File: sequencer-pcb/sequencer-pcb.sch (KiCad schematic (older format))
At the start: 39 parts, among them SW1 SW_Push, SW10 SW_Push, SW11 SW_Push, SW2 SW_Push, SW3 SW_Push, SW4 SW_Push, SW5 SW_Push, SW6 SW_Push, SW7 SW_Push, SW8 SW_Push, SW9 SW_Push, U1 STM32F103C8Tx

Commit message: pcb changes
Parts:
- removed U?: 4051, symbol 4xxx:4051
- added J?: Conn_01x02_Female, symbol Connector:Conn_01x02_Female
- added J?: Conn_02x10_Counter_Clockwise, symbol Connector_Generic:Conn_02x10_Counter_Clockwise
- added J?: Conn_02x08_Counter_Clockwise, symbol Connector_Generic:Conn_02x08_Counter_Clockwise
- added R? (x17): R, symbol Device:R
- added RV?: R_POT_TRIM, symbol Device:R_POT_TRIM
- added TP? (x2): TestPoint, symbol Connector:TestPoint
- added U?: 74HC164, symbol 74xx:74HC164
- renumbered RV3 to RV2, RV5 to RV3, RV7 to RV4, RV2 to RV5, RV4 to RV6, RV6 to RV7
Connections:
- net labels added: +5V, GND, L1, L2, L3, L4, L5, L6, L7, L8, R1, R2, R3, R4, R5, R6, R7, R8
- wire segments 0 -> 123
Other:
- moved on the sheet: D1, D2, D3, D4, D5, D6, D7, D8, D9, J?, RV1, RV10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

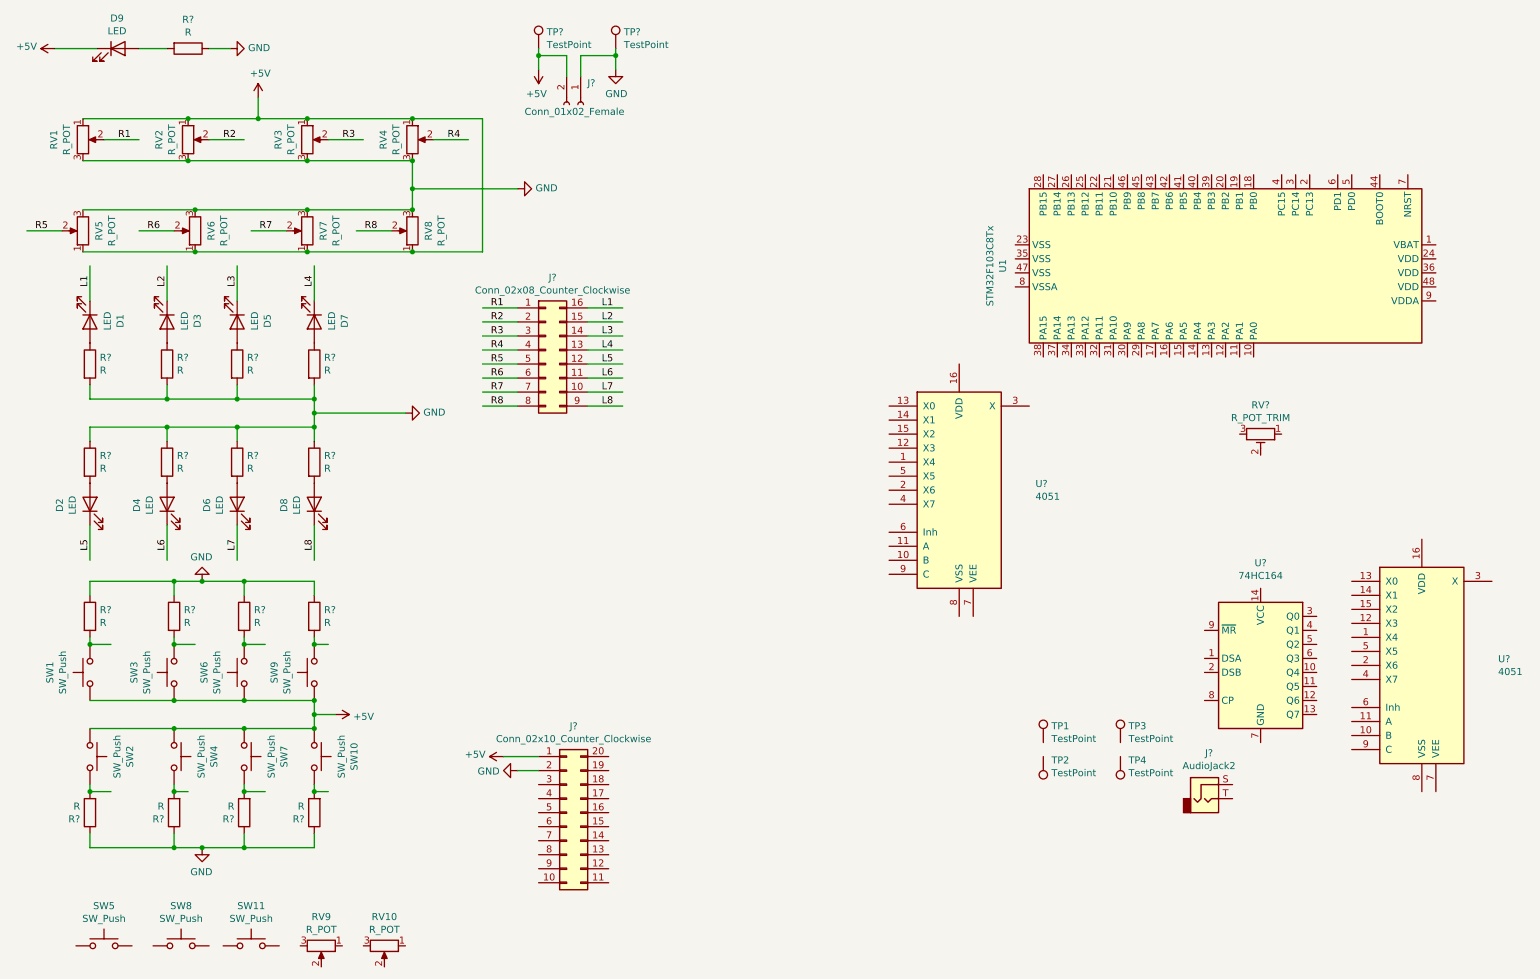
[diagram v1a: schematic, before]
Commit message: updates pcb and schematic
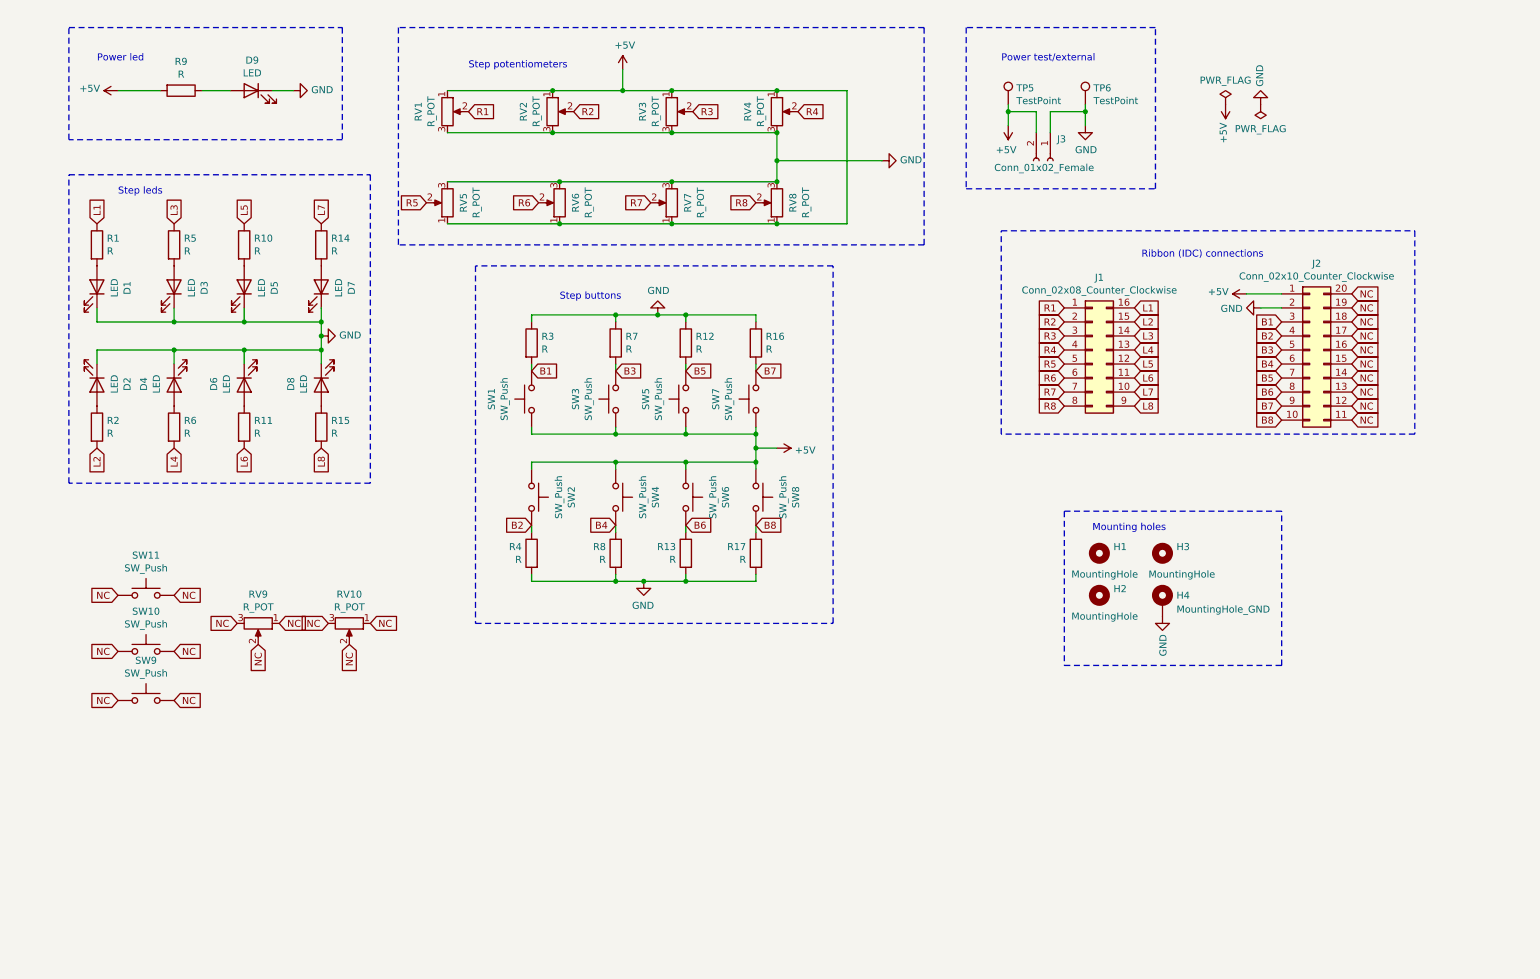
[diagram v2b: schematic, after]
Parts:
- removed J?: AudioJack2, symbol Connector:AudioJack2
- removed J?: Conn_02x10_Counter_Clockwise, symbol Connector_Generic:Conn_02x10_Counter_Clockwise
- removed J?: Conn_02x08_Counter_Clockwise, symbol Connector_Generic:Conn_02x08_Counter_Clockwise
- removed RV?: R_POT_TRIM, symbol Device:R_POT_TRIM
- removed SW5, SW8: SW_Push, symbol Switch:SW_Push
- removed TP1, TP2, TP3, TP4: TestPoint, symbol Connector:TestPoint
- removed U1: STM32F103C8Tx, Package_QFP:LQFP-48_7x7mm_P0.5mm, symbol MCU_ST_STM32F1:STM32F103C8Tx
- removed U? (x2): 4051, symbol 4xxx:4051
- removed U?: 74HC164, symbol 74xx:74HC164
- added H1, H2, H3: MountingHole, MountingHole:MountingHole_2.7mm_M2.5, symbol Mechanical:MountingHole
- added H4: MountingHole_GND, MountingHole:MountingHole_2.7mm_M2.5_Pad, symbol Mechanical:MountingHole_Pad
- added J1: Conn_02x08_Counter_Clockwise, Connector_IDC:IDC-Header_2x08_P2.54mm_Vertical, symbol Connector_Generic:Conn_02x08_Counter_Clockwise
- added J2: Conn_02x10_Counter_Clockwise, Connector_IDC:IDC-Header_2x10_P2.54mm_Vertical, symbol Connector_Generic:Conn_02x10_Counter_Clockwise
- added SW10, SW9: SW_Push, Button_Switch_THT:SW_PUSH_6mm, symbol Switch:SW_Push
- D1, D2, D3, D4, D5, D6, D7, D8, D9: footprint (none) -> LED_THT:LED_D5.0mm
- J3: renamed from J?; footprint (none) -> Connector_PinHeader_2.54mm:PinHeader_1x02_P2.54mm_Vertical
- R1, R10, R11, R12, R13, R14, R15, R16, R17, R2, R3, R4, R5, R6, R7, R8, R9: renamed from R?; footprint (none) -> Resistor_SMD:R_1806_4516Metric_Pad1.57x1.80mm_HandSolder
- RV1, RV10, RV2, RV3, RV4, RV5, RV6, RV7, RV8, RV9: footprint (none) -> Potentiometer_THT:Potentiometer_Alps_RK09K_Single_Vertical
- SW1, SW11, SW2, SW3, SW4: footprint (none) -> Button_Switch_THT:SW_PUSH_6mm
- SW5: renamed from SW6; footprint (none) -> Button_Switch_THT:SW_PUSH_6mm
- SW6: renamed from SW7; footprint (none) -> Button_Switch_THT:SW_PUSH_6mm
- SW7: renamed from SW9; footprint (none) -> Button_Switch_THT:SW_PUSH_6mm
- SW8: renamed from SW10; footprint (none) -> Button_Switch_THT:SW_PUSH_6mm
- TP5, TP6: renamed from TP?; footprint (none) -> TestPoint:TestPoint_THTPad_2.5x2.5mm_Drill1.2mm
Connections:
- net labels added: B1, B2, B3, B4, B5, B6, B7, B8, NC
- wire segments 123 -> 90
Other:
- note added: "Mounting holes\n"
- note added: "Power led"
- note added: "Power test/external"
- note added: "Ribbon (IDC) connections"
- note added: "Step buttons"
- note added: "Step leds"
- note added: "Step potentiometers"
- moved on the sheet: D1, D2, D3, D4, D5, D6, D7, D8, D9, J3, R1, R10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

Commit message: updates
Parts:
- added RV11: R_POT, Potentiometer_THT:Potentiometer_Alps_RK09K_Single_Vertical, symbol Device:R_POT
- added SW12, SW13: SW_Push, Button_Switch_THT:SW_PUSH_6mm, symbol Switch:SW_Push
- J1: value Conn_02x08_Counter_Clockwise -> Ribbon; footprint Connector_IDC:IDC-Header_2x08_P2.54mm_Vertical -> Connector_IDC:IDC-Header_2x10_P2.54mm_Vertical; symbol Connector_Generic:Conn_02x08_Counter_Clockwise -> Connector_Generic:Conn_02x10_Counter_Clockwise
- RV1, RV2, RV3, RV4, RV5, RV6, RV7, RV8: value R_POT -> 100k
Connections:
- net +5V: now also J1.17 (Pin_17); no longer J2.1 (Pin_1)
- net B1: now also J2.1 (Pin_1); no longer J2.3 (Pin_3)
- net B2: now also J2.2 (Pin_2); no longer J2.4 (Pin_4)
- net B3: now also J2.3 (Pin_3); no longer J2.5 (Pin_5)
- net B4: now also J2.4 (Pin_4); no longer J2.6 (Pin_6)
- net B5: now also J2.5 (Pin_5); no longer J2.7 (Pin_7)
- net B6: now also J2.6 (Pin_6); no longer J2.8 (Pin_8)
- net B7: now also J2.7 (Pin_7); no longer J2.9 (Pin_9)
- net B8: now also J2.8 (Pin_8); no longer J2.10 (Pin_10)
- net GND: now also J1.18 (Pin_18); no longer J2.2 (Pin_2)
- net L1: now also J1.9 (Pin_9); no longer J1.16 (Pin_16)
- net L2: now also J1.10 (Pin_10); no longer J1.15 (Pin_15)
- net L3: now also J1.11 (Pin_11); no longer J1.14 (Pin_14)
- net L4: now also J1.12 (Pin_12); no longer J1.13 (Pin_13)
- net L5: now also J1.13 (Pin_13); no longer J1.12 (Pin_12)
- net L6: now also J1.14 (Pin_14); no longer J1.11 (Pin_11)
- net L7: now also J1.15 (Pin_15); no longer J1.10 (Pin_10)
- net L8: now also J1.16 (Pin_16); no longer J1.9 (Pin_9)
- net NC: now also J1.19 (Pin_19), J1.20 (Pin_20), J2.10 (Pin_10), J2.9 (Pin_9), RV11.1, RV11.2, RV11.3, SW12.1, SW12.2, SW13.1, SW13.2
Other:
- moved on the sheet: SW10, SW11, SW9
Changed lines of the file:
@@
 L Switch:SW_Push SW11
 U 1 1 5F2CD552
-P 1500 4750
-F 0 "SW11" H 1500 5035 50  0000 C CNN
-F 1 "SW_Push" H 1500 4944 50  0000 C CNN
-F 2 "Button_Switch_THT:SW_PUSH_6mm" H 1500 4950 50  0001 C CNN
-F 3 "~" H 1500 4950 50  0001 C CNN
-	1    1500 4750
+P 1450 5650
+F 0 "SW11" H 1450 5935 50  0000 C CNN
+F 1 "SW_Push" H 1450 5844 50  0000 C CNN
+F 2 "Button_Switch_THT:SW_PUSH_6mm" H 1450 5850 50  0001 C CNN
+F 3 "~" H 1450 5850 50  0001 C CNN
+	1    1450 5650
 	1    0    0    -1
 $EndComp
@@
 P 6000 1950
 F 0 "RV8" V 5885 1950 50  0000 C CNN
-F 1 "R_POT" V 5794 1950 50  0000 C CNN
+F 1 "100k" V 5794 1950 50  0000 C CNN
 F 2 "Potentiometer_THT:Potentiometer_Alps_RK09K_Single_Vertical" H 6000 1950 50  0001 C CNN
 F 3 "~" H 6000 1950 50  0001 C CNN
@@
 P 5250 1950
 F 0 "RV7" V 5135 1950 50  0000 C CNN
-F 1 "R_POT" V 5044 1950 50  0000 C CNN
+F 1 "100k" V 5044 1950 50  0000 C CNN
 F 2 "Potentiometer_THT:Potentiometer_Alps_RK09K_Single_Vertical" H 5250 1950 50  0001 C CNN
 F 3 "~" H 5250 1950 50  0001 C CNN
@@
 P 4450 1950
 F 0 "RV6" V 4335 1950 50  0000 C CNN
-F 1 "R_POT" V 4244 1950 50  0000 C CNN
+F 1 "100k" V 4244 1950 50  0000 C CNN
 F 2 "Potentiometer_THT:Potentiometer_Alps_RK09K_Single_Vertical" H 4450 1950 50  0001 C CNN
 F 3 "~" H 4450 1950 50  0001 C CNN
@@
 P 3650 1950
 F 0 "RV5" V 3535 1950 50  0000 C CNN
-F 1 "R_POT" V 3444 1950 50  0000 C CNN
+F 1 "100k" V 3444 1950 50  0000 C CNN
 F 2 "Potentiometer_THT:Potentiometer_Alps_RK09K_Single_Vertical" H 3650 1950 50  0001 C CNN
 F 3 "~" H 3650 1950 50  0001 C CNN
@@
 P 6000 1300
 F 0 "RV4" V 5793 1300 50  0000 C CNN
-F 1 "R_POT" V 5884 1300 50  0000 C CNN
+F 1 "100k" V 5884 1300 50  0000 C CNN
 F 2 "Potentiometer_THT:Potentiometer_Alps_RK09K_Single_Vertical" H 6000 1300 50  0001 C CNN
 F 3 "~" H 6000 1300 50  0001 C CNN
@@
 P 5250 1300
 F 0 "RV3" V 5043 1300 50  0000 C CNN
-F 1 "R_POT" V 5134 1300 50  0000 C CNN
+F 1 "100k" V 5134 1300 50  0000 C CNN
 F 2 "Potentiometer_THT:Potentiometer_Alps_RK09K_Single_Vertical" H 5250 1300 50  0001 C CNN
 F 3 "~" H 5250 1300 50  0001 C CNN
@@
 P 4400 1300
 F 0 "RV2" V 4193 1300 50  0000 C CNN
-F 1 "R_POT" V 4284 1300 50  0000 C CNN
+F 1 "100k" V 4284 1300 50  0000 C CNN
 F 2 "Potentiometer_THT:Potentiometer_Alps_RK09K_Single_Vertical" H 4400 1300 50  0001 C CNN
 F 3 "~" H 4400 1300 50  0001 C CNN
@@
 P 3650 1300
 F 0 "RV1" V 3443 1300 50  0000 C CNN
-F 1 "R_POT" V 3534 1300 50  0000 C CNN
+F 1 "100k" V 3534 1300 50  0000 C CNN
 F 2 "Potentiometer_THT:Potentiometer_Alps_RK09K_Single_Vertical" H 3650 1300 50  0001 C CNN
 F 3 "~" H 3650 1300 50  0001 C CNN
@@
 L power:GND #PWR03
 U 1 1 5F407ABC
-P 9450 2700
+P 8700 2700
 AR Path="/5F407ABC" Ref="#PWR03"  Part="1"
 AR Path="/5F3DFCD9/5F407ABC" Ref="#PWR?"  Part="1"
-F 0 "#PWR03" H 9450 2450 50  0001 C CNN
-F 1 "GND" V 9455 2572 50  0000 R CNN
-F 2 "" H 9450 2700 50  0001 C CNN
-F 3 "" H 9450 2700 50  0001 C CNN
-	1    9450 2700
-	0    1    1    0
-$EndComp
-Wire Wire Line
-	9600 2700 9450 2700
-Wire Wire Line
-	9350 2600 9600 2600
+F 0 "#PWR03" H 8700 2450 50  0001 C CNN
+F 1 "GND" V 8705 2572 50  0000 R CNN
+F 2 "" H 8700 2700 50  0001 C CNN
+F 3 "" H 8700 2700 50  0001 C CNN
+	1    8700 2700
+	0    -1   -1   0
+$EndComp
+Wire Wire Line
+	8550 2700 8700 2700
+Wire Wire Line
+	8800 2800 8550 2800
 $Comp
 L power:+5V #PWR02
 U 1 1 5F407AC4
-P 9350 2600
+P 8800 2800
 AR Path="/5F407AC4" Ref="#PWR02"  Part="1"
 AR Path="/5F3DFCD9/5F407AC4" Ref="#PWR?"  Part="1"
-F 0 "#PWR02" H 9350 2450 50  0001 C CNN
-F 1 "+5V" V 9365 2728 50  0000 L CNN
-F 2 "" H 9350 2600 50  0001 C CNN
-F 3 "" H 9350 2600 50  0001 C CNN
-	1    9350 2600
-	0    -1   -1   0
-$EndComp
-$Comp
-L Connector_Generic:Conn_02x08_Counter_Clockwise J1
+F 0 "#PWR02" H 8800 2650 50  0001 C CNN
+F 1 "+5V" V 8815 2928 50  0000 L CNN
+F 2 "" H 8800 2800 50  0001 C CNN
+F 3 "" H 8800 2800 50  0001 C CNN
+	1    8800 2800
+	0    1    1    0
+$EndComp
+$Comp
+L Connector_Generic:Conn_02x10_Counter_Clockwise J1
 U 1 1 5F407ACA
-P 8250 3000
+P 8250 2900
 AR Path="/5F407ACA" Ref="J1"  Part="1"
 AR Path="/5F3DFCD9/5F407ACA" Ref="J?"  Part="1"
-F 0 "J1" H 8300 3517 50  0000 C CNN
-F 1 "Conn_02x08_Counter_Clockwise" H 8300 3426 50  0000 C CNN
-F 2 "Connector_IDC:IDC-Header_2x08_P2.54mm_Vertical" H 8250 3000 50  0001 C CNN
-F 3 "~" H 8250 3000 50  0001 C CNN
-	1    8250 3000
+F 0 "J1" H 8300 3417 50  0000 C CNN
+F 1 "Ribbon" H 8300 3326 50  0000 C CNN
+F 2 "Connector_IDC:IDC-Header_2x10_P2.54mm_Vertical" H 8250 2900 50  0001 C CNN
+F 3 "~" H 8250 2900 50  0001 C CNN
+	1    8250 2900
 	1    0    0    -1
 $EndComp
@@
 	1    0    0    -1
 $EndComp
+Text GLabel 8050 2500 0    50   Input ~ 0
+R1
+Text GLabel 8050 2600 0    50   Input ~ 0
+R2
 Text GLabel 8050 2700 0    50   Input ~ 0
-R1
+R3
 Text GLabel 8050 2800 0    50   Input ~ 0
-R2
+R4
 Text GLabel 8050 2900 0    50   Input ~ 0
-R3
+R5
 Text GLabel 8050 3000 0    50   Input ~ 0
-R4
+R6
 Text GLabel 8050 3100 0    50   Input ~ 0
-R5
+R7
 Text GLabel 8050 3200 0    50   Input ~ 0
-R6
+R8
 Text GLabel 8050 3300 0    50   Input ~ 0
-R7
+L1
 Text GLabel 8050 3400 0    50   Input ~ 0
-R8
-Text GLabel 8550 2700 2    50   Input ~ 0
-L1
-Text GLabel 8550 2800 2    50   Input ~ 0
 L2
+Text GLabel 8550 3400 2    50   Input ~ 0
+L3
+Text GLabel 8550 3300 2    50   Input ~ 0
+L4
+Text GLabel 8550 3200 2    50   Input ~ 0
+L5
+Text GLabel 8550 3100 2    50   Input ~ 0
+L6
+Text GLabel 8550 3000 2    50   Input ~ 0
+L7
 Text GLabel 8550 2900 2    50   Input ~ 0
-L3
-Text GLabel 8550 3000 2    50   Input ~ 0
-L4
-Text GLabel 8550 3100 2    50   Input ~ 0
-L5
-Text GLabel 8550 3200 2    50   Input ~ 0
-L6
-Text GLabel 8550 3300 2    50   Input ~ 0
-L7
-Text GLabel 8550 3400 2    50   Input ~ 0
 L8
+Text GLabel 9600 2600 0    50   Input ~ 0
+B1
+Text GLabel 9600 2700 0    50   Input ~ 0
+B2
 Text GLabel 9600 2800 0    50   Input ~ 0
-B1
+B3
 Text GLabel 9600 2900 0    50   Input ~ 0
-B2
+B4
 Text GLabel 9600 3000 0    50   Input ~ 0
-B3
+B5
 Text GLabel 9600 3100 0    50   Input ~ 0
-B4
+B6
 Text GLabel 9600 3200 0    50   Input ~ 0
-B5
+B7
 Text GLabel 9600 3300 0    50   Input ~ 0
-B6
-Text GLabel 9600 3400 0    50   Input ~ 0
-B7
-Text GLabel 9600 3500 0    50   Input ~ 0
 B8
 Text Notes 1150 950  0    50   ~ 0
@@
 	10550 2150 10550 3600
 Wire Notes Line
-	10550 3600 7600 3600
+	7600 3600 10550 3600
 Wire Notes Line
 	7600 3600 7600 2150
@@
 Text GLabel 2150 4950 0    50   Input ~ 0
 NC
-Text GLabel 1700 4750 2    50   Input ~ 0
-NC
-Text GLabel 1300 4750 0    50   Input ~ 0
+Text GLabel 1650 5650 2    50   Input ~ 0
+NC
+Text GLabel 1250 5650 0    50   Input ~ 0
 NC
 $Comp
 L Switch:SW_Push SW10
 U 1 1 5F506B13
-P 1500 5150
-F 0 "SW10" H 1500 5435 50  0000 C CNN
-F 1 "SW_Push" H 1500 5344 50  0000 C CNN
-F 2 "Button_Switch_THT:SW_PUSH_6mm" H 1500 5350 50  0001 C CNN
-F 3 "~" H 1500 5350 50  0001 C CNN
-	1    1500 5150
-	1    0    0    -1
-$EndComp
-Text GLabel 1700 5150 2    50   Input ~ 0
-NC
-Text GLabel 1300 5150 0    50   Input ~ 0
+P 1450 6050
+F 0 "SW10" H 1450 6335 50  0000 C CNN
+F 1 "SW_Push" H 1450 6244 50  0000 C CNN
+F 2 "Button_Switch_THT:SW_PUSH_6mm" H 1450 6250 50  0001 C CNN
+F 3 "~" H 1450 6250 50  0001 C CNN
+	1    1450 6050
+	1    0    0    -1
+$EndComp
+Text GLabel 1650 6050 2    50   Input ~ 0
+NC
+Text GLabel 1250 6050 0    50   Input ~ 0
 NC
 $Comp
 L Switch:SW_Push SW9
 U 1 1 5F50971E
-P 1500 5500
-F 0 "SW9" H 1500 5785 50  0000 C CNN
-F 1 "SW_Push" H 1500 5694 50  0000 C CNN
-F 2 "Button_Switch_THT:SW_PUSH_6mm" H 1500 5700 50  0001 C CNN
-F 3 "~" H 1500 5700 50  0001 C CNN
-	1    1500 5500
-	1    0    0    -1
-$EndComp
-Text GLabel 1700 5500 2    50   Input ~ 0
-NC
-Text GLabel 1300 5500 0    50   Input ~ 0
+P 1450 6400
+F 0 "SW9" H 1450 6685 50  0000 C CNN
+F 1 "SW_Push" H 1450 6594 50  0000 C CNN
+F 2 "Button_Switch_THT:SW_PUSH_6mm" H 1450 6600 50  0001 C CNN
+F 3 "~" H 1450 6600 50  0001 C CNN
+	1    1450 6400
+	1    0    0    -1
+$EndComp
+Text GLabel 1650 6400 2    50   Input ~ 0
+NC
+Text GLabel 1250 6400 0    50   Input ~ 0
 NC
 $Comp
@@
 Wire Wire Line
 	5850 3100 5850 3150
+$Comp
+L Switch:SW_Push SW13
+U 1 1 5F31C72E
+P 1450 5300
+F 0 "SW13" H 1450 5585 50  0000 C CNN
+F 1 "SW_Push" H 1450 5494 50  0000 C CNN
+F 2 "Button_Switch_THT:SW_PUSH_6mm" H 1450 5500 50  0001 C CNN
+F 3 "~" H 1450 5500 50  0001 C CNN
+	1    1450 5300
+	1    0    0    -1
+$EndComp
+Text GLabel 1650 5300 2    50   Input ~ 0
+NC
+Text GLabel 1250 5300 0    50   Input ~ 0
+NC
+$Comp
+L Switch:SW_Push SW12
+U 1 1 5F32393D
+P 1450 4900
+F 0 "SW12" H 1450 5185 50  0000 C CNN
+F 1 "SW_Push" H 1450 5094 50  0000 C CNN
+F 2 "Button_Switch_THT:SW_PUSH_6mm" H 1450 5100 50  0001 C CNN
+F 3 "~" H 1450 5100 50  0001 C CNN
+	1    1450 4900
+	1    0    0    -1
+$EndComp
+Text GLabel 1650 4900 2    50   Input ~ 0
+NC
+Text GLabel 1250 4900 0    50   Input ~ 0
+NC
+$Comp
+L Device:R_POT RV11
+U 1 1 5F326108
+P 2650 5450
+F 0 "RV11" V 2443 5450 50  0000 C CNN
+F 1 "R_POT" V 2534 5450 50  0000 C CNN
+F 2 "Potentiometer_THT:Potentiometer_Alps_RK09K_Single_Vertical" H 2650 5450 50  0001 C CNN
+F 3 "~" H 2650 5450 50  0001 C CNN
+	1    2650 5450
+	0    1    1    0
+$EndComp
+Text GLabel 2800 5450 2    50   Input ~ 0
+NC
+Text GLabel 2650 5600 3    50   Input ~ 0
+NC
+Text GLabel 2500 5450 0    50   Input ~ 0
+NC
+Text GLabel 9600 3400 0    50   Input ~ 0
+NC
+Text GLabel 9600 3500 0    50   Input ~ 0
+NC
+Text GLabel 8550 2600 2    50   Input ~ 0
+NC
+Text GLabel 8550 2500 2    50   Input ~ 0
+NC
 $EndSCHEMATC
